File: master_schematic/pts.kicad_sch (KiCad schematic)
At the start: 10 parts

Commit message: PT update
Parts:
- added R1, R10, R13, R16, R19, R22, R25, R28, R4, R7: 330, symbol Device:R
- added R11, R12, R14, R15, R17, R18, R2, R20, R21, R23, R24, R26, R27, R29, R3, R30, R5, R6, R8, R9: 470, symbol Device:R
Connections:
- net GND: now also R12.2, R15.2, R18.2, R21.2, R24.2, R27.2, R3.2, R30.2, R6.2, R9.2
- net PT1_I: now also R16.2, R17.1; no longer PT6.3 (DATA)
- net PT1_N: now also R4.2, R5.1; no longer PT2.3 (DATA)
- net PT1_O: now also R1.2, R2.1; no longer PT1.3 (DATA)
- net PT1_P: now also R10.2, R11.1; no longer PT4.3 (DATA)
- net PT1_T: now also R13.2, R14.1; no longer PT5.3 (DATA)
- net PT2_I: now also R19.2, R20.1; no longer PT7.3 (DATA)
- net PT2_N: now also R7.2, R8.1; no longer PT3.3 (DATA)
- net PT3_I: now also R22.2, R23.1; no longer PT8.3 (DATA)
- net PT4_I: now also R25.2, R26.1; no longer PT9.3 (DATA)
- net PT5_I: now also R28.2, R29.1; no longer PT10.3 (DATA)
- net 5V renamed +5V
- new net: R17.2, R18.1
- new net: R5.2, R6.1
- new net: R29.2, R30.1
- new net: R23.2, R24.1
- new net: R2.2, R3.1
- new net: R20.2, R21.1
- new net: R14.2, R15.1
- new net: R8.2, R9.1
- new net: R11.2, R12.1
- new net: R26.2, R27.1
- new net PT1_I_RAW: PT6.3 (DATA), R16.1
- new net PT1_N_RAW: PT2.3 (DATA), R4.1
- new net PT1_O_RAW: PT1.3 (DATA), R1.1
- new net PT1_P_RAW: PT4.3 (DATA), R10.1
- new net PT1_T_RAW: PT5.3 (DATA), R13.1
- new net PT2_I_RAW: PT7.3 (DATA), R19.1
- new net PT2_N_RAW: PT3.3 (DATA), R7.1
- new net PT3_I_RAW: PT8.3 (DATA), R22.1
- new net PT4_I_RAW: PT9.3 (DATA), R25.1
- new net PT5_I_RAW: PT10.3 (DATA), R28.1

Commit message: modified for PCB development
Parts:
- removed PT10: ~, hb_footprint_lib:Pressure Transducer (Low), symbol hb_symbol_lib:pressure_transducer
- removed R21, R23, R24, R26, R27, R29, R30, R5, R6: 470, symbol Device:R
- removed R22, R25, R28: 330, symbol Device:R
- PT1, PT2, PT3, PT4, PT5, PT6, PT7, PT8, PT9: footprint hb_footprint_lib:Pressure Transducer (Low) -> hb_footprint_lib:CONN_SD-43045-001_04_MOL
- R1, R13, R19, R7: value 330 -> 1K
- R10, R16, R4: value 330 -> 2.7K
- R11, R15, R17, R3, R9: value 470 -> 1K
- R12, R14, R18, R2, R20, R8: value 470 -> 2.7K
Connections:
- net PT2_N is gone; now on net PT1_P: R7.2, R8.1
- net GND: now also R10.2, R14.2, R16.2, R2.2, R20.2, R4.2, R8.2; no longer R15.2, R3.2, R9.2
- net PT1_I: now also R11.2, R12.1; no longer R16.2, R17.1
- net PT1_I_RAW: now also R11.1; no longer R16.1
- net PT1_N: now also R3.2, R4.1; no longer R4.2
- net PT1_N_RAW: now also R3.1; no longer R4.1
- net PT1_P: no longer R10.2, R11.1
- net PT1_P_RAW: now also R7.1; no longer R10.1
- net PT1_T: now also R10.1, R9.2; no longer R13.2, R14.1
- net PT1_T_RAW: now also R9.1; no longer R13.1
- net PT2_I: now also R13.2, R14.1; no longer R19.2, R20.1
- net PT2_I_RAW: now also R13.1; no longer R19.1
- net PT3_I: now also R15.2, R16.1
- net PT3_I_RAW: now also R15.1
- net PT4_I: now also R17.2, R18.1
- net PT4_I_RAW: now also R17.1
- net PT5_I: now also R19.2, R20.1
- net PT5_I_RAW: now also PT3.3 (DATA), R19.1
- removed net PT2_N_RAW: PT3.3 (DATA), R7.1
- no-connect marks 10 -> 9

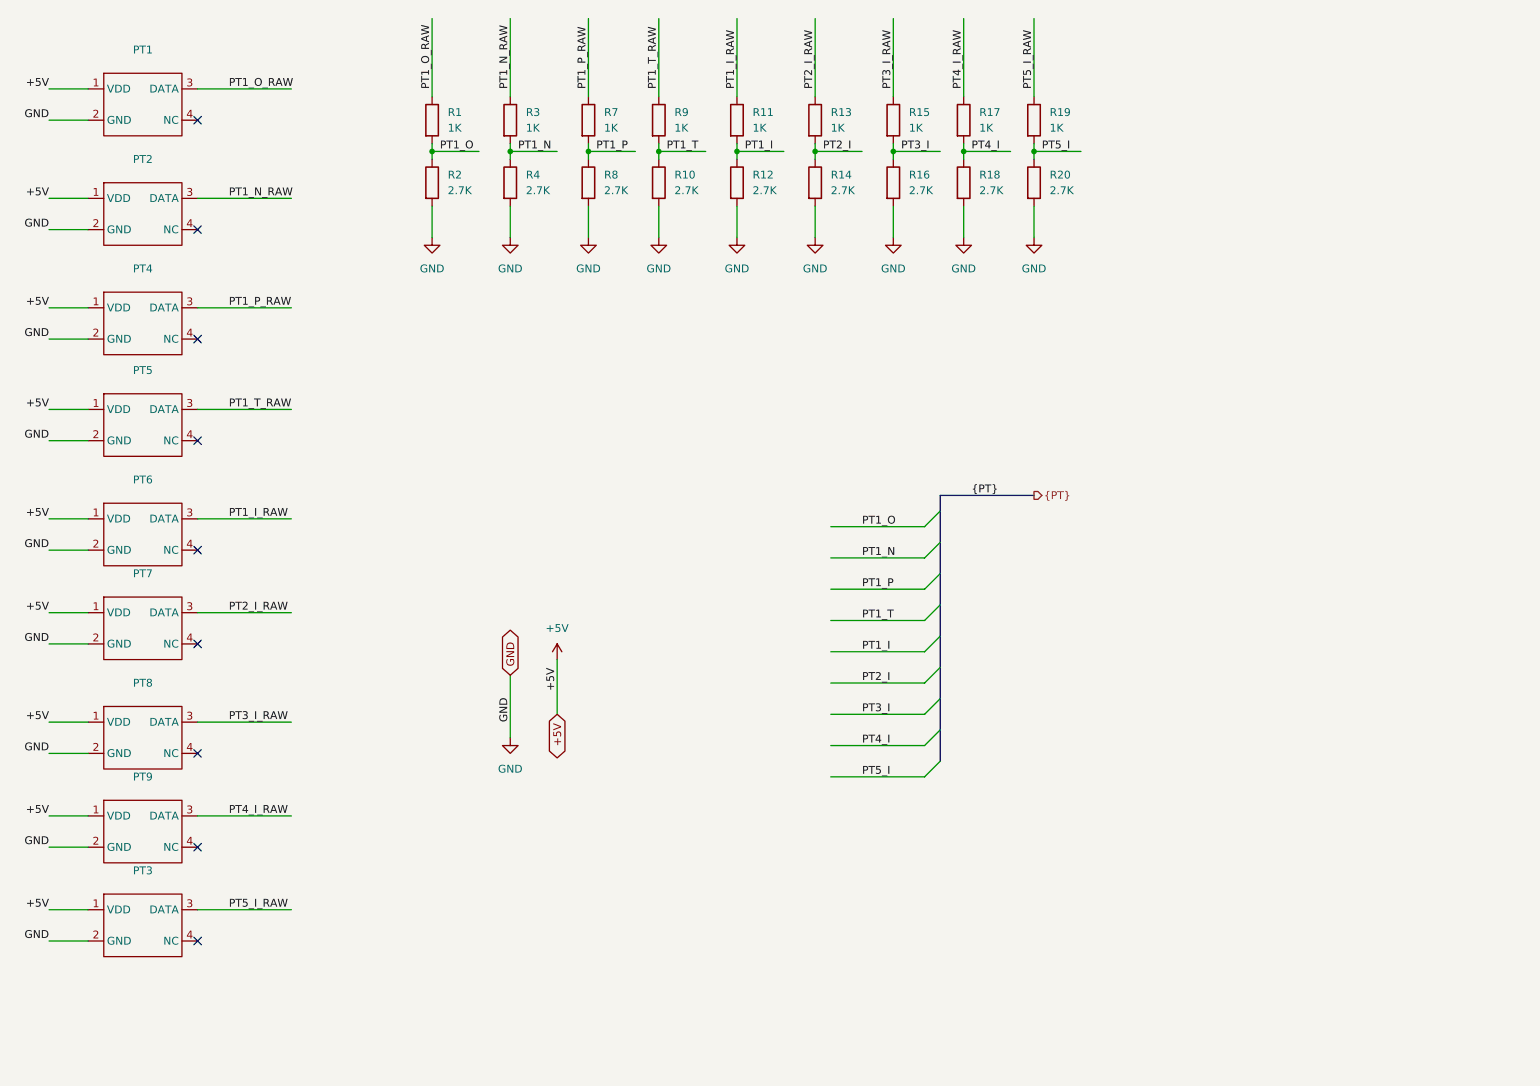
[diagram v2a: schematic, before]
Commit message: updated with part info
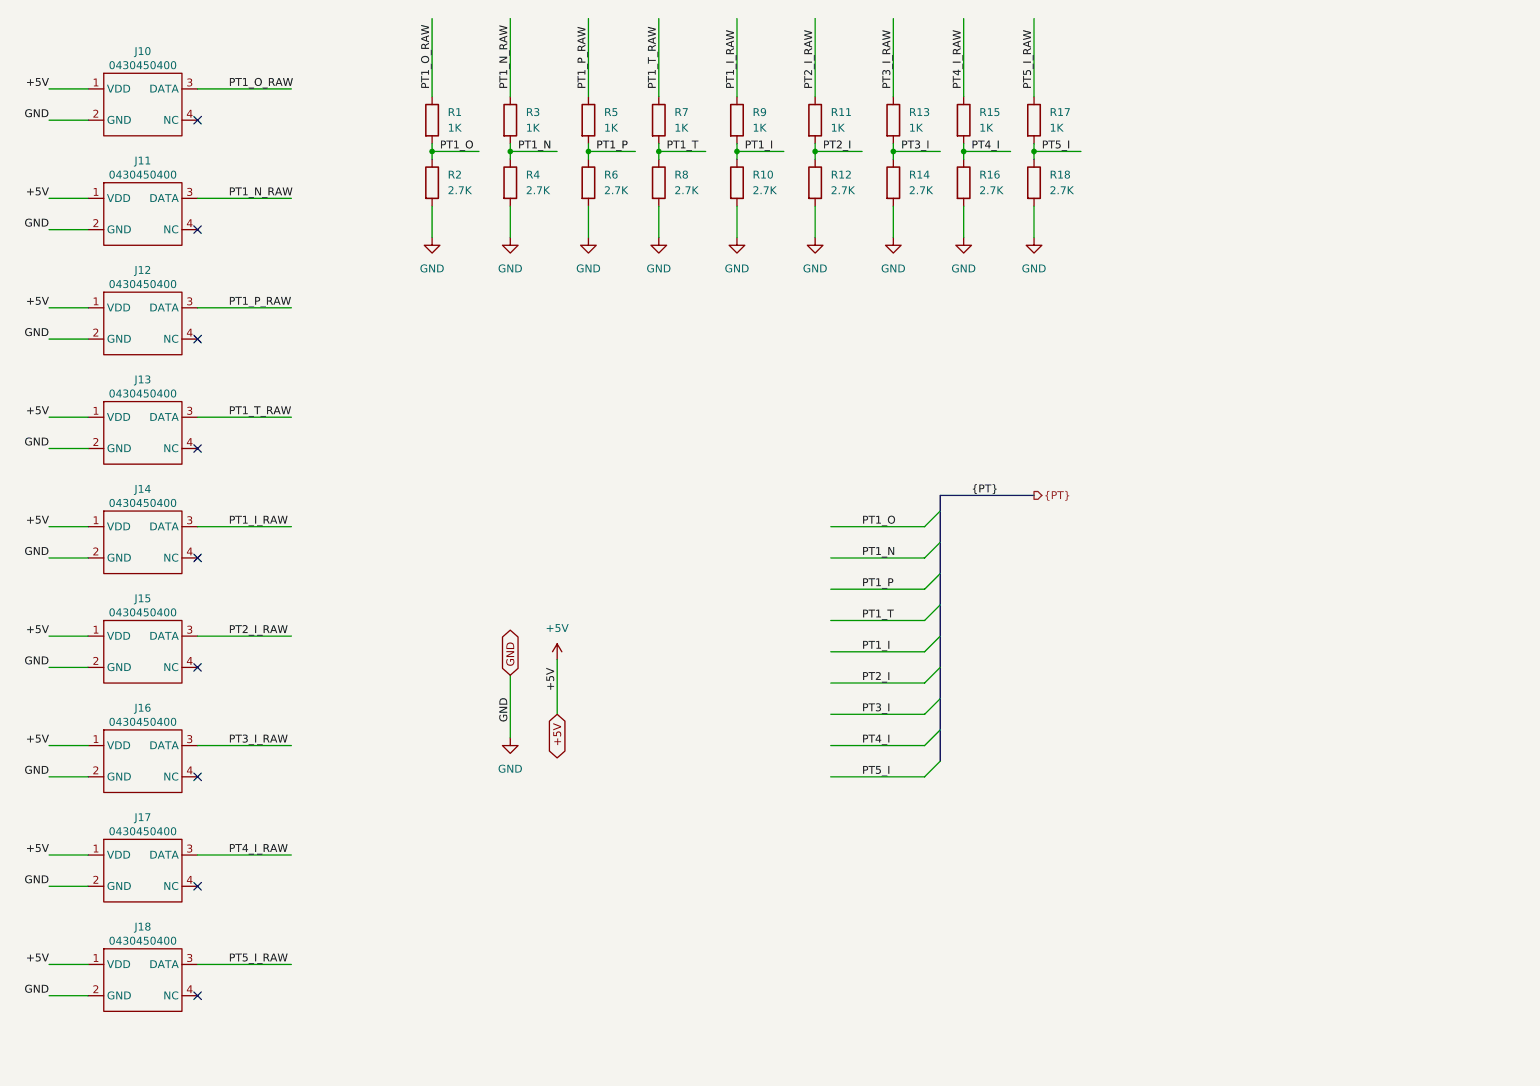
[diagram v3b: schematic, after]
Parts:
- removed PT2, PT3, PT4, PT5, PT6, PT7, PT8, PT9: ~, hb_footprint_lib:CONN_SD-43045-001_04_MOL, symbol hb_symbol_lib:pressure_transducer
- removed R19: 1K, symbol Device:R
- removed R20: 2.7K, symbol Device:R
- added J11, J12, J13, J14, J15, J16, J17, J18: 0430450400, hb_footprint_lib:CONN_SD-43045-001_04_MOL, symbol hb_symbol_lib:pressure_transducer
- added R5: 1K, Resistor_SMD:R_0805_2012Metric_Pad1.20x1.40mm_HandSolder, symbol Device:R
- added R6: 2.7K, Resistor_SMD:R_0805_2012Metric_Pad1.20x1.40mm_HandSolder, symbol Device:R
- J10: renamed from PT1; value ~ -> 0430450400; Cost @ Qty (none) -> 1.42; Manufacturer (none) -> Molex; Manufacturer Part # (none) -> 0430450400; Supplier (none) -> Digikey; Supplier Part # (none) -> WM1814-ND; Unit Cost (none) -> 1.42
- R1, R11, R13, R15, R17, R3, R7, R9: footprint (none) -> Resistor_SMD:R_0805_2012Metric_Pad1.20x1.40mm_HandSolder; Cost @ Qty (none) -> 0.066; Manufacturer (none) -> Panasonic Electronic Components; Manufacturer Part # (none) -> ERA-6AEB102V; Supplier (none) -> Digikey; Supplier Part # (none) -> P1.0KDACT-ND; Unit Cost (none) -> 0.10
- R10, R12, R14, R16, R18, R2, R4, R8: footprint (none) -> Resistor_SMD:R_0805_2012Metric_Pad1.20x1.40mm_HandSolder; Cost @ Qty (none) -> 0.042; Manufacturer (none) -> Panasonic Electronic Components; Manufacturer Part # (none) -> ERJ-6GEYJ272V; Supplier (none) -> Digikey; Supplier Part # (none) -> P2.7KACT-ND; Unit Cost (none) -> 0.10
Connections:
- net +5V: now also J11.1 (VDD), J12.1 (VDD), J13.1 (VDD), J14.1 (VDD), J15.1 (VDD), J16.1 (VDD), J17.1 (VDD), J18.1 (VDD)
- net GND: now also J11.2 (GND), J12.2 (GND), J13.2 (GND), J14.2 (GND), J15.2 (GND), J16.2 (GND), J17.2 (GND), J18.2 (GND), R6.2
- net PT1_I: now also R10.1, R9.2; no longer R11.2, R12.1
- net PT1_I_RAW: now also R9.1, J14.3 (DATA); no longer R11.1
- net PT1_N_RAW: now also J11.3 (DATA)
- net PT1_P: now also R5.2, R6.1; no longer R7.2, R8.1
- net PT1_P_RAW: now also J12.3 (DATA), R5.1; no longer R7.1
- net PT1_T: now also R7.2, R8.1; no longer R10.1, R9.2
- net PT1_T_RAW: now also R7.1, J13.3 (DATA); no longer R9.1
- net PT2_I: now also R11.2, R12.1; no longer R13.2, R14.1
- net PT2_I_RAW: now also R11.1, J15.3 (DATA); no longer R13.1
- net PT3_I: now also R13.2, R14.1; no longer R15.2, R16.1
- net PT3_I_RAW: now also R13.1, J16.3 (DATA); no longer R15.1
- net PT4_I: now also R15.2, R16.1; no longer R17.2, R18.1
- net PT4_I_RAW: now also R15.1, J17.3 (DATA); no longer R17.1
- net PT5_I: now also R17.2, R18.1
- net PT5_I_RAW: now also R17.1, J18.3 (DATA)

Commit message: fixed errors on schematic
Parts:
- renumbered J18 to J10, J10 to J2, J11 to J3, J12 to J4, J13 to J5, J14 to J6, J15 to J7, J16 to J8, J17 to J9
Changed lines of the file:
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@@
 		(dnp no)
 		(fields_autoplaced yes)
-		(property "Reference" "J10"
+		(property "Reference" "J2"
 			(at 55.88 25.654 0)
 			(effects
@@
 			(project "master_schematic"
 				(path "/c4f7e98c-e88d-49cc-9841-b70710a90a72/666fb9f9-c631-4136-ad00-30a1b375897d"
-					(reference "J10")
+					(reference "J2")
 					(unit 1)
 				)
@@
 		(dnp no)
 		(fields_autoplaced yes)
-		(property "Reference" "J17"
+		(property "Reference" "J9"
 			(at 55.88 150.114 0)
 			(effects
@@
 			(project "master_schematic"
 				(path "/c4f7e98c-e88d-49cc-9841-b70710a90a72/666fb9f9-c631-4136-ad00-30a1b375897d"
-					(reference "J17")
+					(reference "J9")
 					(unit 1)
 				)
@@
 		(dnp no)
 		(fields_autoplaced yes)
-		(property "Reference" "J15"
+		(property "Reference" "J7"
 			(at 55.88 114.554 0)
 			(effects
@@
 			(project "master_schematic"
 				(path "/c4f7e98c-e88d-49cc-9841-b70710a90a72/666fb9f9-c631-4136-ad00-30a1b375897d"
-					(reference "J15")
+					(reference "J7")
 					(unit 1)
 				)
@@
 		(dnp no)
 		(fields_autoplaced yes)
-		(property "Reference" "#PWR011"
+		(property "Reference" "#PWR024"
 			(at 189.23 62.23 0)
 			(effects
@@
 			(project "master_schematic"
 				(path "/c4f7e98c-e88d-49cc-9841-b70710a90a72/666fb9f9-c631-4136-ad00-30a1b375897d"
-					(reference "#PWR011")
+					(reference "#PWR024")
 					(unit 1)
 				)
@@
 		(dnp no)
 		(fields_autoplaced yes)
-		(property "Reference" "#PWR09"
+		(property "Reference" "#PWR022"
 			(at 165.1 62.23 0)
 			(effects
@@
 			(project "master_schematic"
 				(path "/c4f7e98c-e88d-49cc-9841-b70710a90a72/666fb9f9-c631-4136-ad00-30a1b375897d"
-					(reference "#PWR09")
+					(reference "#PWR022")
 					(unit 1)
 				)
@@
 		(dnp no)
 		(fields_autoplaced yes)
-		(property "Reference" "#PWR08"
+		(property "Reference" "#PWR021"
 			(at 152.4 62.23 0)
 			(effects
@@
 			(project "master_schematic"
 				(path "/c4f7e98c-e88d-49cc-9841-b70710a90a72/666fb9f9-c631-4136-ad00-30a1b375897d"
-					(reference "#PWR08")
+					(reference "#PWR021")
 					(unit 1)
 				)
@@
 		(dnp no)
 		(fields_autoplaced yes)
-		(property "Reference" "#PWR07"
+		(property "Reference" "#PWR020"
 			(at 139.7 62.23 0)
 			(effects
@@
 			(project "master_schematic"
 				(path "/c4f7e98c-e88d-49cc-9841-b70710a90a72/666fb9f9-c631-4136-ad00-30a1b375897d"
-					(reference "#PWR07")
+					(reference "#PWR020")
 					(unit 1)
 				)
@@
 		(dnp no)
 		(fields_autoplaced yes)
-		(property "Reference" "#PWR014"
+		(property "Reference" "#PWR018"
 			(at 123.19 128.27 0)
 			(effects
@@
 		)
 		(instances
-			(project ""
+			(project "master_schematic"
 				(path "/c4f7e98c-e88d-49cc-9841-b70710a90a72/666fb9f9-c631-4136-ad00-30a1b375897d"
-					(reference "#PWR014")
+					(reference "#PWR018")
 					(unit 1)
 				)
@@
 		(dnp no)
 		(fields_autoplaced yes)
-		(property "Reference" "J12"
+		(property "Reference" "J4"
 			(at 55.88 61.214 0)
 			(effects
@@
 			(project "master_schematic"
 				(path "/c4f7e98c-e88d-49cc-9841-b70710a90a72/666fb9f9-c631-4136-ad00-30a1b375897d"
-					(reference "J12")
+					(reference "J4")
 					(unit 1)
 				)
@@
 		(dnp no)
 		(fields_autoplaced yes)
-		(property "Reference" "#PWR04"
+		(property "Reference" "#PWR016"
 			(at 115.57 62.23 0)
 			(effects
@@
 			(project "master_schematic"
 				(path "/c4f7e98c-e88d-49cc-9841-b70710a90a72/666fb9f9-c631-4136-ad00-30a1b375897d"
-					(reference "#PWR04")
+					(reference "#PWR016")
 					(unit 1)
 				)
@@
 		(dnp no)
 		(fields_autoplaced yes)
-		(property "Reference" "#PWR012"
+		(property "Reference" "#PWR025"
 			(at 200.66 62.23 0)
 			(effects
@@
 			(project "master_schematic"
 				(path "/c4f7e98c-e88d-49cc-9841-b70710a90a72/666fb9f9-c631-4136-ad00-30a1b375897d"
-					(reference "#PWR012")
+					(reference "#PWR025")
 					(unit 1)
 				)
@@
 		(dnp no)
 		(fields_autoplaced yes)
-		(property "Reference" "J14"
+		(property "Reference" "J6"
 			(at 55.88 96.774 0)
 			(effects
@@
 			(project "master_schematic"
 				(path "/c4f7e98c-e88d-49cc-9841-b70710a90a72/666fb9f9-c631-4136-ad00-30a1b375897d"
-					(reference "J14")
+					(reference "J6")
 					(unit 1)
 				)
@@
 		(dnp no)
 		(fields_autoplaced yes)
-		(property "Reference" "#PWR010"
+		(property "Reference" "#PWR023"
 			(at 177.8 62.23 0)
 			(effects
@@
 			(project "master_schematic"
 				(path "/c4f7e98c-e88d-49cc-9841-b70710a90a72/666fb9f9-c631-4136-ad00-30a1b375897d"
-					(reference "#PWR010")
+					(reference "#PWR023")
 					(unit 1)
 				)
@@
 		(dnp no)
 		(fields_autoplaced yes)
-		(property "Reference" "#PWR03"
+		(property "Reference" "#PWR015"
 			(at 102.87 62.23 0)
 			(effects
@@
 			(project "master_schematic"
 				(path "/c4f7e98c-e88d-49cc-9841-b70710a90a72/666fb9f9-c631-4136-ad00-30a1b375897d"
-					(reference "#PWR03")
+					(reference "#PWR015")
 					(unit 1)
 				)
@@
 		)
 		(instances
-			(project ""
+			(project "master_schematic"
 				(path "/c4f7e98c-e88d-49cc-9841-b70710a90a72/666fb9f9-c631-4136-ad00-30a1b375897d"
 					(reference "R1")
@@
 		(dnp no)
 		(fields_autoplaced yes)
-		(property "Reference" "J13"
+		(property "Reference" "J5"
 			(at 55.88 78.994 0)
 			(effects
@@
 			(project "master_schematic"
 				(path "/c4f7e98c-e88d-49cc-9841-b70710a90a72/666fb9f9-c631-4136-ad00-30a1b375897d"
-					(reference "J13")
+					(reference "J5")
 					(unit 1)
 				)
@@
 		(dnp no)
 		(fields_autoplaced yes)
-		(property "Reference" "#PWR06"
+		(property "Reference" "#PWR019"
 			(at 128.27 62.23 0)
 			(effects
@@
 			(project "master_schematic"
 				(path "/c4f7e98c-e88d-49cc-9841-b70710a90a72/666fb9f9-c631-4136-ad00-30a1b375897d"
-					(reference "#PWR06")
+					(reference "#PWR019")
 					(unit 1)
 				)
@@
 		(dnp no)
 		(fields_autoplaced yes)
-		(property "Reference" "J16"
+		(property "Reference" "J8"
 			(at 55.88 132.334 0)
 			(effects
@@
 			(project "master_schematic"
 				(path "/c4f7e98c-e88d-49cc-9841-b70710a90a72/666fb9f9-c631-4136-ad00-30a1b375897d"
-					(reference "J16")
+					(reference "J8")
 					(unit 1)
 				)
@@
 		(dnp no)
 		(fields_autoplaced yes)
-		(property "Reference" "J11"
+		(property "Reference" "J3"
 			(at 55.88 43.434 0)
 			(effects
@@
 			(project "master_schematic"
 				(path "/c4f7e98c-e88d-49cc-9841-b70710a90a72/666fb9f9-c631-4136-ad00-30a1b375897d"
-					(reference "J11")
+					(reference "J3")
 					(unit 1)
 				)
@@
 		(on_board yes)
 		(dnp no)
-		(property "Reference" "J18"
+		(property "Reference" "J10"
 			(at 55.88 167.894 0)
 			(effects
@@
 			(project "master_schematic"
 				(path "/c4f7e98c-e88d-49cc-9841-b70710a90a72/666fb9f9-c631-4136-ad00-30a1b375897d"
-					(reference "J18")
+					(reference "J10")
 					(unit 1)
 				)
@@
 		(dnp no)
 		(fields_autoplaced yes)
-		(property "Reference" "#PWR013"
+		(property "Reference" "#PWR017"
 			(at 115.57 143.51 0)
 			(effects
@@
 		)
 		(instances
-			(project ""
+			(project "master_schematic"
 				(path "/c4f7e98c-e88d-49cc-9841-b70710a90a72/666fb9f9-c631-4136-ad00-30a1b375897d"
-					(reference "#PWR013")
+					(reference "#PWR017")
 					(unit 1)
 				)
